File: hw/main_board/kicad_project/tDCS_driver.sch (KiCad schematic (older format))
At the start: 57 parts, among them P1 CONN_5, P2 CONN_5, P3 CONN_6, P4 CONN_8, P5 CONN_8, U1 MAX338, U2 SI5351A, U3 AD5292, U4 AD8221, U5 MAX339, U6 OP1177, U7 MAX338, X1 CRYSTAL6-10pf

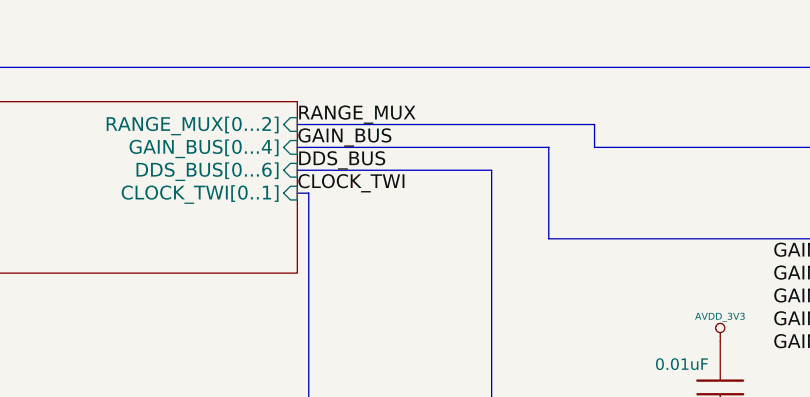
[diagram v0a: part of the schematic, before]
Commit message: PWR_board hierarchy added
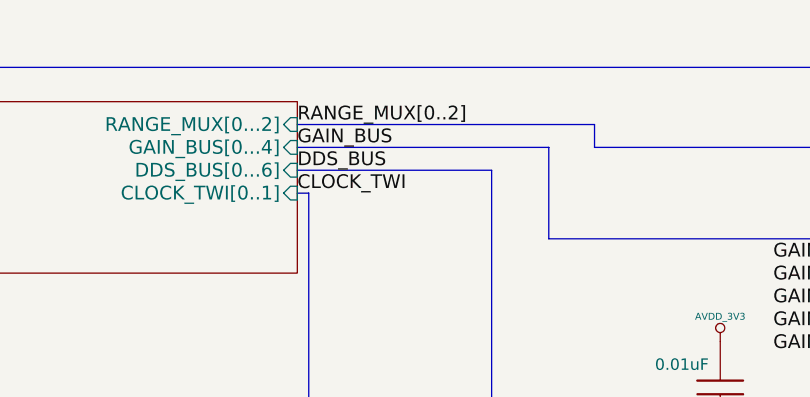
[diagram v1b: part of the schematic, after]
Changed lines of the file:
@@
 LIBS:ddslib
 LIBS:demuxcomplib
-LIBS:noname-cache
-EELAYER 27 0
+LIBS:tDCS_driver-cache
+EELAYER 24 0
 EELAYER END
 $Descr A4 11693 8268
@@
 Sheet 1 3
 Title "noname.sch"
-Date "25 jan 2014"
+Date "26 feb 2014"
 Rev ""
 Comp ""
@@
 IN_MUX
 Text Label 3250 1100 0    60   ~ 0
-RANGE_MUX
+RANGE_MUX[0..2]
 Text Label 3250 1200 0    60   ~ 0
 GAIN_BUS
